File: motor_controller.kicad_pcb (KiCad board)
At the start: 4 copper layers, 43.7 x 46.5 mm, 35 parts, among them IC1 DRV8304SRHAR, J1 PWM, J2 SPI, J3 MISC, J4 PWR IN, J5 MOTOR, Q1 CSD18514Q5A, Q2 CSD18514Q5A, Q3 CSD18514Q5A, Q4 CSD18514Q5A, Q5 CSD18514Q5A, Q6 CSD18514Q5A

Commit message: added lib
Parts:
- IC1: footprint SamacSys_Parts:QFN50P600X600X100-41N-D -> kicad_library:QFN50P600X600X100-41N-D
- J1, J3: footprint SamacSys_Parts:JST-6PIN -> kicad_library:JST-6PIN
- J2: footprint SamacSys_Parts:JST-4PIN -> kicad_library:JST-4PIN
- Q1, Q2, Q3, Q4, Q5, Q6: footprint SamacSys_Parts:CSD18514Q5A -> kicad_library:CSD18514Q5A
- R3, R4, R5: value SHUNT -> 1-10m ohm
- R6: value 10 -> 62

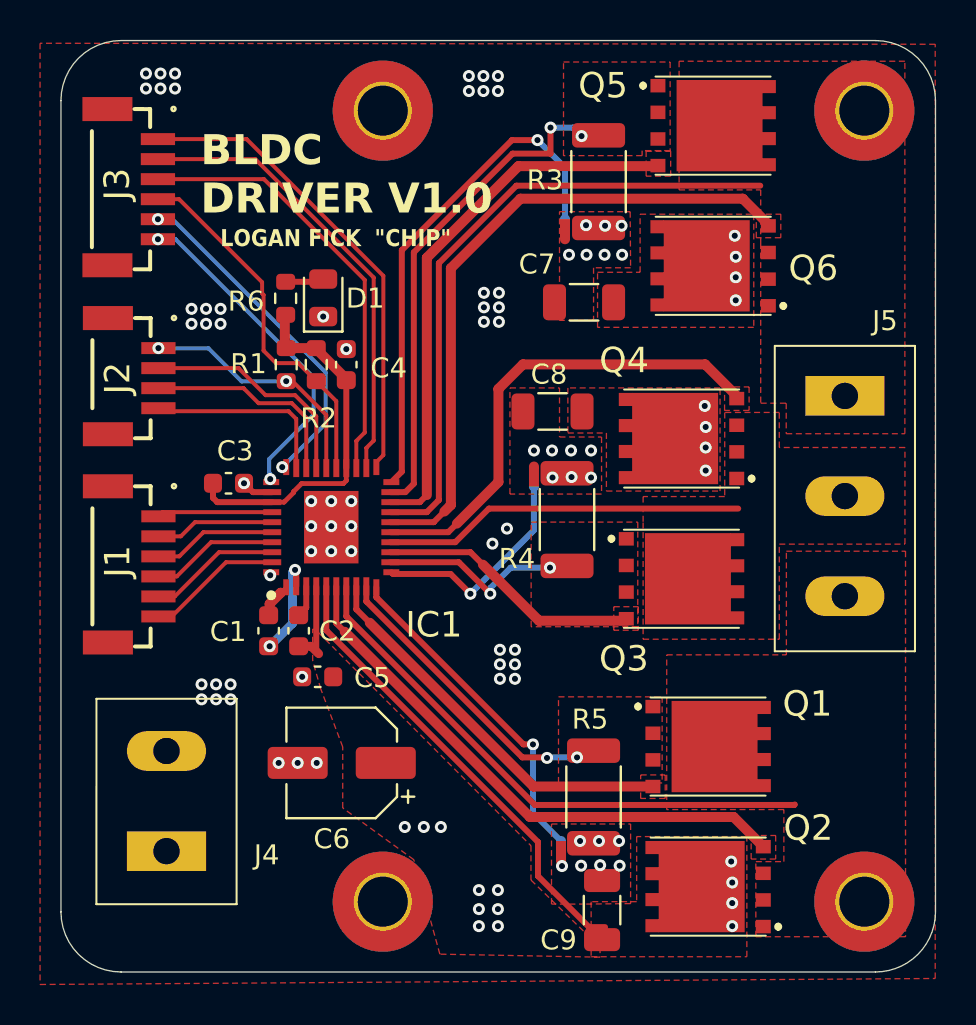
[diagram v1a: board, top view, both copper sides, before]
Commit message: added electrolytic bulk and changed footprint sizes of other decoupling caps to match digikey sizes
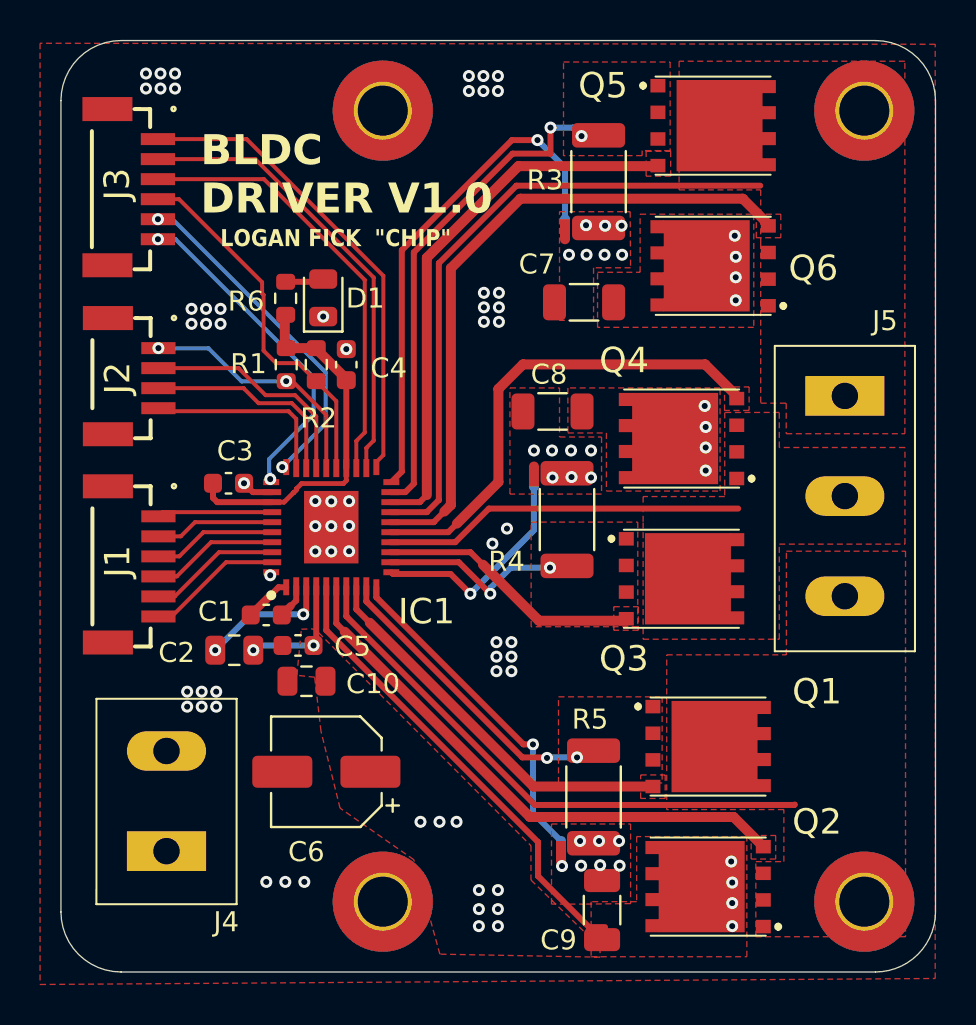
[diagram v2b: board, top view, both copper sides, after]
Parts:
- added C10: 47 uF (VM), Capacitor_SMD:C_0805_2012Metric, F.Cu at (164.9, 81.4)
- C2: footprint Capacitor_SMD:C_0603_1608Metric -> Capacitor_SMD:C_0805_2012Metric
- moved C2 3.36 mm to (161.3, 79.8), turned to 180 degrees
- moved C5 1.85 mm to (164.5, 79.6)
- moved C6 0.89 mm to (165.9, 85.9)
- moved C1 0.80 mm to (162.9, 78.1), turned to 180 degrees
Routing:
- net Net-(IC1-VCP): track 1.60 -> 6.60 mm, vias 0 -> 2
- net Net-(IC1-CPH): track 5.21 -> 2.08 mm, vias 2 -> 0
- net VM: track 28.0 -> 29.4 mm, vias 21 -> 23
- net Net-(IC1-CPL): track 1.76 -> 2.34 mm
- net GND: vias 76 -> 75

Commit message: added digikey footprint for bulk cap
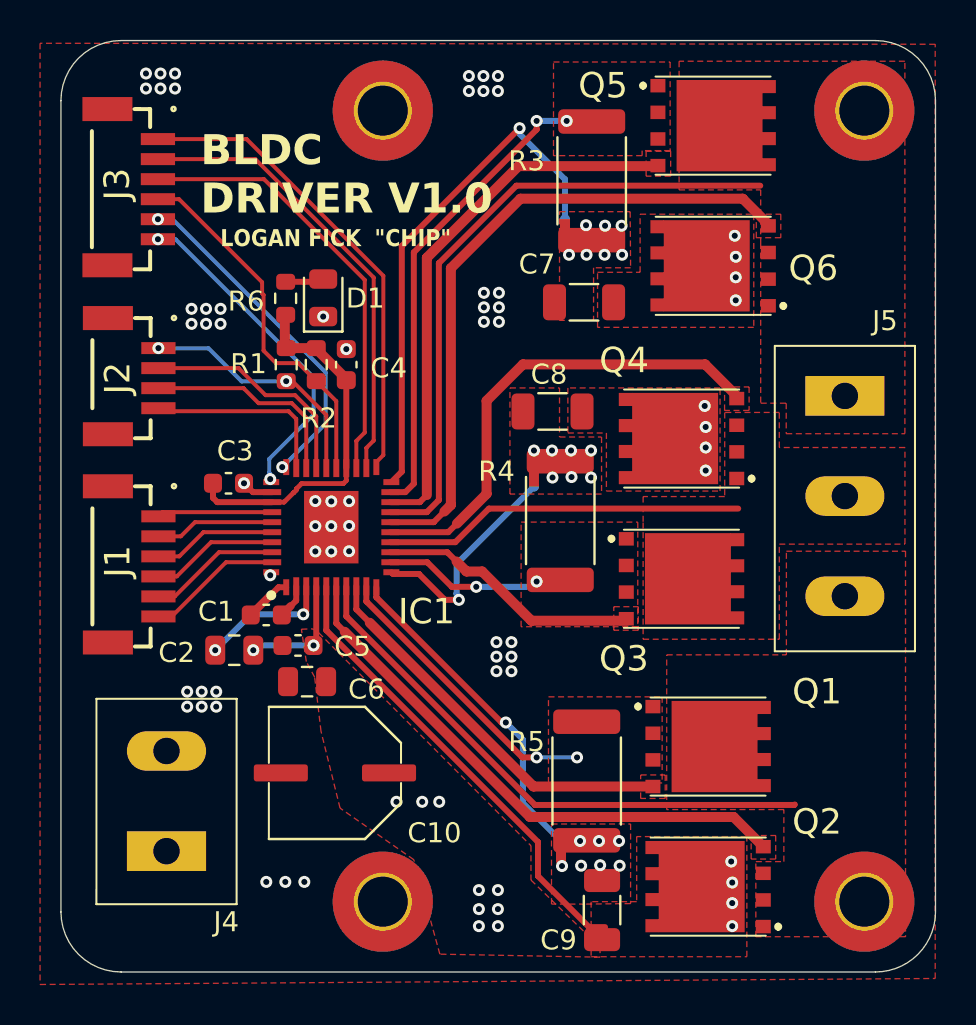
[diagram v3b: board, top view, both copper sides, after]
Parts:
- C10: footprint Capacitor_SMD:C_0805_2012Metric -> kicad_library:6.6x6.6 cap
- C6: footprint Capacitor_SMD:CP_Elec_5x5.4 -> Capacitor_SMD:C_0805_2012Metric
- R3, R4, R5: footprint Resistor_SMD:R_2010_5025Metric -> Resistor_SMD:R_2512_6332Metric
- moved C10 4.80 mm to (166.3, 86.0), turned to 0 degrees
- moved C6 4.60 mm to (164.9, 81.4)
- moved R5 0.87 mm to (178.9, 86.4)
- moved R3 0.35 mm to (179.1, 56.4)
- moved R4 0.34 mm to (177.6, 73.3)
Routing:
- net /SPB: track 9.66 -> 7.92 mm
- net /SPC: track 24.8 -> 23.2 mm
- net GND: vias 75 -> 73

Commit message: final rev 1.0
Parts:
- moved J5 0.61 mm to (192.4, 67.1)
- moved J4 0.52 mm to (157.4, 89.9)
